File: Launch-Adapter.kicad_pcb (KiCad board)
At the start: 4 copper layers, 81.8 x 144.5 mm, 96 parts, among them J1 ADC1, J2 ADC2, J3 PWM, J4 GPIO, J5 Driver, J6 Measurements, U1 R-785.0-1.0, U2 R-78C3.3-1.0, U3 ISO1050DUB, U4 ADM3490ExR, U5 LMV324

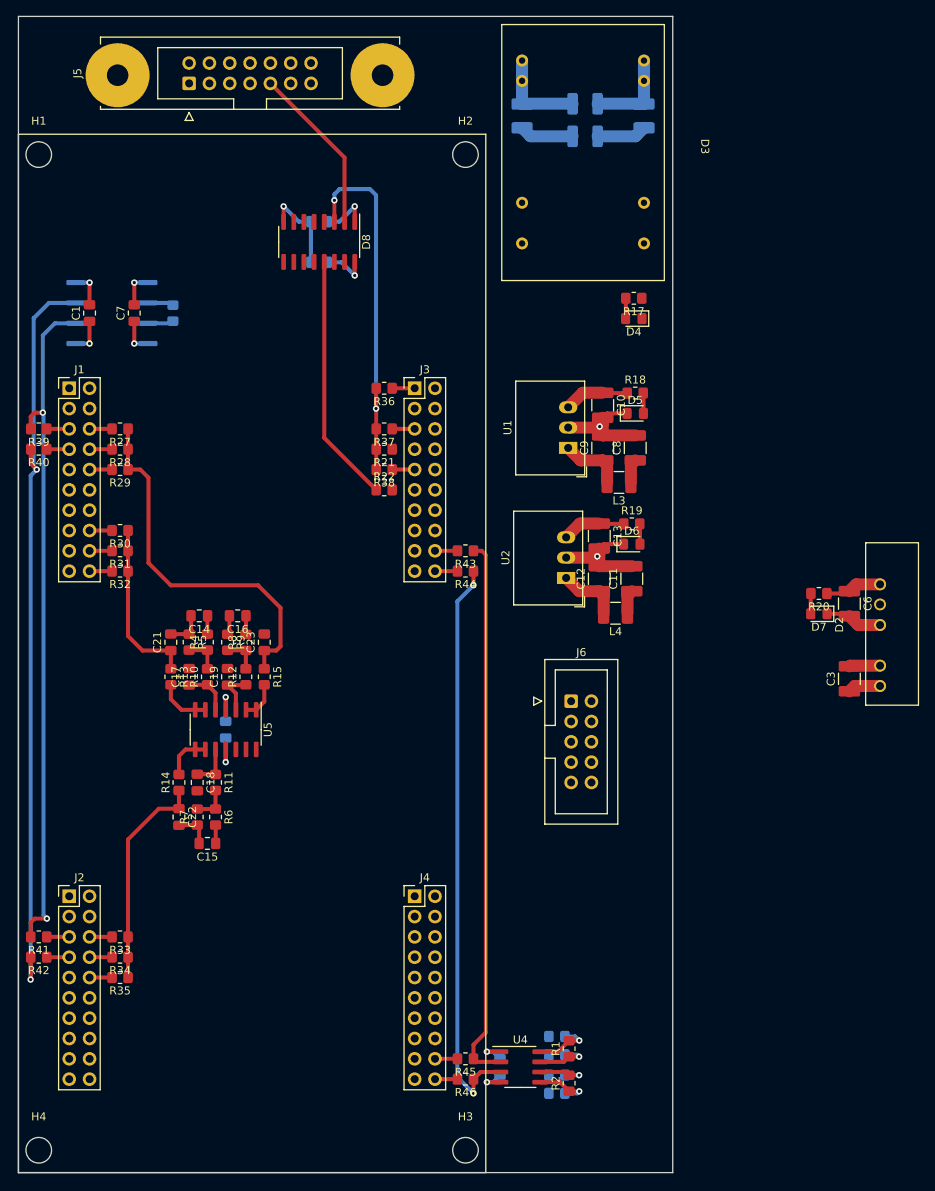
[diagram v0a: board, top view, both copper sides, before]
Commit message: Добавил молексы и убрал питание
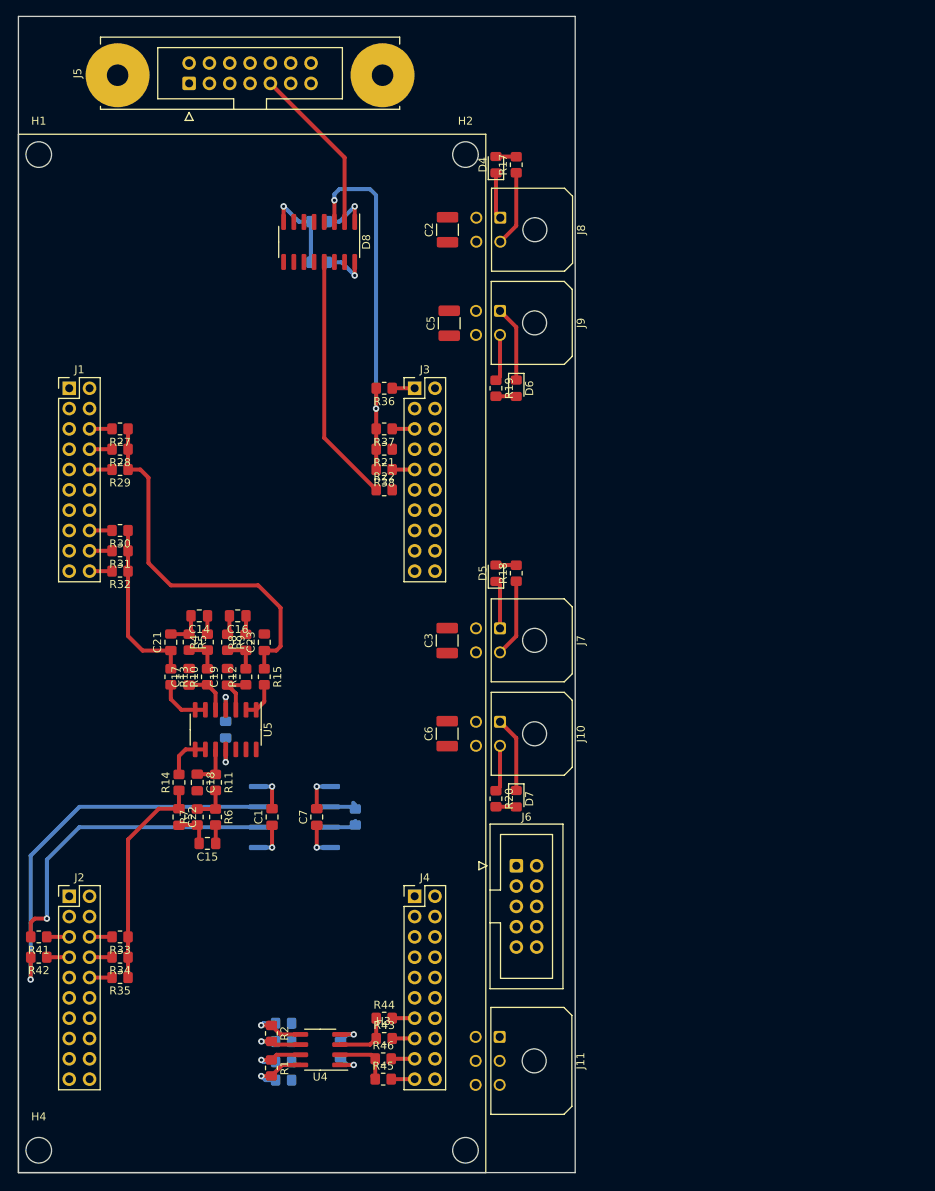
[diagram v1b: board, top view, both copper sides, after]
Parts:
- removed C10, C11, C13, C8: 10u, Capacitor_SMD:C_1210_3225Metric_Pad1.33x2.70mm_HandSolder
- removed C12, C9: 2.2u, Capacitor_SMD:C_1210_3225Metric_Pad1.33x2.70mm_HandSolder
- removed D2: TMA1505S, TRACO_My:TMA1505S
- removed D3: TEN3_2413WI, TRACO_My:TEN3_2413
- removed L1, L2: 150u, Inductor_SMD:L_1210_3225Metric_Pad1.42x2.65mm_HandSolder
- removed L3, L4: 5.6u, Inductor_SMD:L_1210_3225Metric_Pad1.42x2.65mm_HandSolder
- removed R39, R40: 0, Resistor_SMD:R_0805_2012Metric_Pad1.20x1.40mm_HandSolder
- removed U1: R-785.0-1.0, Converter_DCDC:Converter_DCDC_RECOM_R-78E-0.5_THT
- removed U2: R-78C3.3-1.0, Converter_DCDC:Converter_DCDC_RECOM_R-78E-0.5_THT
- added J10: +5V_CAN, Connector_Molex:Molex_Micro-Fit_3.0_43045-0400_2x02_P3.00mm_Horizontal, F.Cu at (116.8, 105.4)
- added J11: Input, Connector_Molex:Molex_Micro-Fit_3.0_43045-0600_2x03_P3.00mm_Horizontal, F.Cu at (116.8, 144.8)
- added J7: +5V, Connector_Molex:Molex_Micro-Fit_3.0_43045-0400_2x02_P3.00mm_Horizontal, F.Cu at (116.8, 93.8)
- added J8: +15V, Connector_Molex:Molex_Micro-Fit_3.0_43045-0400_2x02_P3.00mm_Horizontal, F.Cu at (116.9, 42.4)
- added J9: +3.3V, Connector_Molex:Molex_Micro-Fit_3.0_43045-0400_2x02_P3.00mm_Horizontal, F.Cu at (116.8, 54.1)
- C2, C5: value 4.7u -> 10u; moved to F.Cu
- moved C1 67.0 mm to (88.3, 117.3)
- moved C7 67.0 mm to (93.9, 117.3)
- moved R3 67.0 mm to (98.8, 117.3)
- moved U3 67.0 mm to (91.1, 117.3)
- moved R43 61.8 mm to (102.4, 145.0), turned to 0 degrees
- moved R44 56.8 mm to (102.4, 142.5), turned to 0 degrees
- moved C6 52.8 mm to (110.2, 106.9), turned to 90 degrees
- moved C3 50.5 mm to (110.2, 95.3)
- moved R20 47.8 mm to (116.3, 115.1), turned to -90 degrees
- moved D7 44.3 mm to (118.9, 115.1), turned to -90 degrees
- moved R2 37.7 mm to (88.3, 144.4), turned to -90 degrees
- moved R1 37.3 mm to (88.3, 148.7), turned to -90 degrees
- moved R24 35.3 mm to (89.8, 143.1), turned to 180 degrees
- moved R26 34.6 mm to (89.8, 150.2), turned to 0 degrees
- moved R25 34.4 mm to (89.8, 145.4), turned to 0 degrees
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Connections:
- C2 pad 1: V_IN_SUPPLY -> +15V
- C2 pad 2: GNDD -> GND
- C3 pad 1: +15V -> +5V
- C5 pad 1: Net-(C5-Pad1) -> +3V3
- C5 pad 2: Net-(C5-Pad2) -> GND
- J1 pad 5: Net-(J1-Pad5) -> unconnected-(J1-Pad5)
- J1 pad 7: Net-(J1-Pad7) -> unconnected-(J1-Pad7)
- J3 pad 18: Net-(J3-Pad18) -> unconnected-(J3-Pad18)
- J3 pad 20: Net-(J3-Pad20) -> unconnected-(J3-Pad20)
- J4 pad 13: unconnected-(J4-Pad13) -> Net-(J4-Pad13)
- J4 pad 15: unconnected-(J4-Pad15) -> Net-(J4-Pad15)
- J4 pad 17: unconnected-(J4-Pad17) -> Net-(J4-Pad17)
- J4 pad 18: Net-(J4-Pad18) -> unconnected-(J4-Pad18)
- J4 pad 19: unconnected-(J4-Pad19) -> Net-(J4-Pad19)
- J4 pad 20: Net-(J4-Pad20) -> unconnected-(J4-Pad20)
- R43 pad 1: RO -> DI
- R43 pad 2: Net-(J3-Pad18) -> Net-(J4-Pad15)
- R44 pad 2: Net-(J3-Pad20) -> Net-(J4-Pad13)
- R45 pad 2: Net-(J4-Pad18) -> Net-(J4-Pad19)
- R46 pad 1: DI -> RO
- R46 pad 2: Net-(J4-Pad20) -> Net-(J4-Pad17)
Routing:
- net DI: track 72.5 -> 7.38 mm, vias 2 -> 0
- net RO: track 68.9 -> 7.70 mm
- net RXD: track 85.1 -> 39.5 mm, vias 2 -> 1
- net TXD: track 94.8 -> 49.3 mm, vias 2 -> 1
- net Net-(C5-Pad2): track 11.8 -> 0.00 mm
- net Net-(C5-Pad1): track 11.3 -> 0.00 mm
- net GND: track 67.6 -> 57.3 mm, vias 6 -> 4
- net Net-(C9-Pad1): track 7.95 -> 0.00 mm
- net Net-(C12-Pad1): track 7.81 -> 0.00 mm
- net GNDD: track 6.75 -> 0.00 mm
- net V_IN_SUPPLY: track 6.24 -> 0.00 mm
- net Net-(J4-Pad20): track 2.81 -> 0.00 mm
- net Net-(J4-Pad19): track 0.00 -> 2.81 mm
- net Net-(J4-Pad18): track 2.81 -> 0.00 mm
- net Net-(J4-Pad17): track 0.00 -> 2.81 mm
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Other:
- board size 81.8 x 144.5 mm -> 69.6 x 144.5 mm

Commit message: Первая версия в производство
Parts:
- added D1: PVT412LSPBF, Package_DIP:DIP-6_W8.89mm_SMDSocket_LongPads, F.Cu at (75.4, 45.0)
- added D2: D_Small, Diode_SMD:D_SOD-323F, F.Cu at (79.2, 35.1)
- added J12: Current Measure, Connector_Molex:Molex_Micro-Fit_3.0_43045-0400_2x02_P3.00mm_Horizontal, F.Cu at (126.8, 129.9)
- added J13: Current Measure, Connector_Molex:Molex_Micro-Fit_3.0_43045-0400_2x02_P3.00mm_Horizontal, F.Cu at (126.9, 24.2)
- added Q1: BC817, Package_TO_SOT_SMD:SOT-23, F.Cu at (75.4, 54.6)
- added R16: 4.7k, Resistor_SMD:R_0805_2012Metric_Pad1.20x1.40mm_HandSolder, F.Cu at (74.4, 62.5)
- added R39: 10k, Resistor_SMD:R_0805_2012Metric_Pad1.20x1.40mm_HandSolder, F.Cu at (75.4, 58.7)
- added R40: 220, Resistor_SMD:R_0805_2012Metric_Pad1.20x1.40mm_HandSolder, F.Cu at (71.9, 57.7)
- added R47: 10k, Resistor_SMD:R_0805_2012Metric_Pad1.20x1.40mm_HandSolder, F.Cu at (89.7, 39.4)
- J11: value Input -> Interfaces; footprint Connector_Molex:Molex_Micro-Fit_3.0_43045-0600_2x03_P3.00mm_Horizontal -> Connector_Molex:Molex_Micro-Fit_3.0_43045-0800_2x04_P3.00mm_Horizontal
- J6: value Measurements -> Voltage measure; footprint Connector_IDC:IDC-Header_2x05_P2.54mm_Vertical -> Connector_Molex:Molex_Micro-Fit_3.0_43045-0400_2x02_P3.00mm_Horizontal
- R41: value 0 -> 60
- R42: value 0 -> 10k
- moved R42 102.4 mm to (89.7, 37.1), turned to 0 degrees
- moved R41 90.4 mm to (82.3, 45.0)
- moved R21 38.7 mm to (89.7, 34.8), turned to 0 degrees
- moved D5 21.2 mm to (134.4, 75.7), turned to 0 degrees
- moved R20 19.9 mm to (134.4, 106.7), turned to 0 degrees
- moved D7 19.0 mm to (134.4, 104.1), turned to 0 degrees
- moved D4 18.1 mm to (134.4, 34.0), turned to 0 degrees
- moved R19 18.1 mm to (134.4, 65.3), turned to 0 degrees
- moved R18 17.7 mm to (134.4, 78.2), turned to 0 degrees
- moved R17 15.5 mm to (134.4, 36.6), turned to 0 degrees
- moved D6 15.5 mm to (134.4, 62.7), turned to 0 degrees
- moved C3 14.1 mm to (120.2, 85.3)
- moved C6 14.1 mm to (120.2, 96.9)
- moved J10 14.1 mm to (126.8, 95.4)
- moved J7 14.1 mm to (126.8, 83.8)
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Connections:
- D8 pad 4: unconnected-(D8-Pad4) -> nERR_IN
- D8 pad 5: unconnected-(D8-Pad5) -> nERR_IN_GPIO
- D8 pad 6: unconnected-(D8-Pad6) -> RESET
- D8 pad 7: unconnected-(D8-Pad7) -> RESET_GPIO
- J1 pad 5: unconnected-(J1-Pad5) -> TXD
- J1 pad 7: unconnected-(J1-Pad7) -> RXD
- J11 pad 1: unconnected-(J11-Pad1) -> CANL
- J11 pad 2: unconnected-(J11-Pad2) -> V_IN_PWR
- J11 pad 3: unconnected-(J11-Pad3) -> B
- J11 pad 4: unconnected-(J11-Pad4) -> Y
- J11 pad 5: unconnected-(J11-Pad5) -> CANH
- J11 pad 6: unconnected-(J11-Pad6) -> GNDD
- J2 pad 5: Net-(J2-Pad5) -> unconnected-(J2-Pad5)
- J2 pad 7: Net-(J2-Pad7) -> unconnected-(J2-Pad7)
- J3 pad 13: unconnected-(J3-Pad13) -> RESET_GPIO
- J3 pad 15: unconnected-(J3-Pad15) -> nERR_IN_GPIO
- J3 pad 18: unconnected-(J3-Pad18) -> Relay_Control
- J4 pad 11: unconnected-(J4-Pad11) -> Net-(J4-Pad11)
- J4 pad 17: Net-(J4-Pad17) -> unconnected-(J4-Pad17)
- J4 pad 19: Net-(J4-Pad19) -> unconnected-(J4-Pad19)
- J4 pad 9: unconnected-(J4-Pad9) -> Net-(J4-Pad9)
- J6 pad 1: unconnected-(J6-Pad1) -> GND
- J6 pad 2: unconnected-(J6-Pad2) -> GND
- J6 pad 3: unconnected-(J6-Pad3) -> V_IN
- J6 pad 4: unconnected-(J6-Pad4) -> V_OUT
- R23 pad 1: GND -> GNDD
- R24 pad 1: GND -> GNDD
- R41 pad 1: Net-(J2-Pad5) -> +15V
- R41 pad 2: RXD -> Net-(D1-Pad6)
- R42 pad 1: Net-(J2-Pad7) -> GND
- R42 pad 2: TXD -> nERR_IN_GPIO
- R43 pad 2: Net-(J4-Pad15) -> Net-(J4-Pad11)
- R44 pad 2: Net-(J4-Pad13) -> Net-(J4-Pad9)
- R45 pad 2: Net-(J4-Pad19) -> Net-(J4-Pad15)
- R46 pad 2: Net-(J4-Pad17) -> Net-(J4-Pad13)
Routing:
- net V_IN_PWR: track 0.00 -> 67.9 mm, vias 0 -> 1
- net Relay_Control: track 0.00 -> 65.4 mm
- net nERR_IN_GPIO: track 0.00 -> 63.9 mm, vias 0 -> 1
- net Y: track 7.26 -> 68.7 mm
- net V_OUT: track 2.29 -> 60.7 mm, vias 0 -> 1
- net RESET_GPIO: track 0.00 -> 54.0 mm, vias 0 -> 1
- net Z: track 6.85 -> 60.8 mm
- net I_INDUCT: track 2.31 -> 55.6 mm
- net B: track 7.02 -> 60.0 mm
- net V_IN: track 2.33 -> 54.7 mm, vias 0 -> 1
- net GNDD: track 0.00 -> 49.4 mm, vias 0 -> 1
- net CANL: track 3.21 -> 50.5 mm
- net A: track 7.47 -> 52.5 mm
- net CANH: track 3.21 -> 46.5 mm
- net GND: track 57.3 -> 93.5 mm, vias 4 -> 20
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- added copper zone on F.Cu, net +15V
- added copper zone on F.Cu, net +3V3
- added copper zone on In1.Cu, net +3V3
- added copper zone on F.Cu, net +5V
- added copper zone on In2.Cu, net +5V
- added copper zone on F.Cu, net +5VD
- added copper zone on B.Cu, net GND
- added copper zone on F.Cu, net GND
- added copper zone on F.Cu, net GND2
- added copper zone on In1.Cu, net Net-(D1-Pad4)
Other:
- board size 69.6 x 144.5 mm -> 80.3 x 142.5 mm
- board text added: "+"
- board text added: "+15V"
- board text added: "+3.3V"
- board text added: "+5V"
- board text added: "-"
- board text added: "5V CAN"
- board text added: "Current Measure"
- board text added: "Driver Connector"
- board text added: "RS-485/CAN"
- board text added: "Relay"
- board text added: "Voltage Measure"

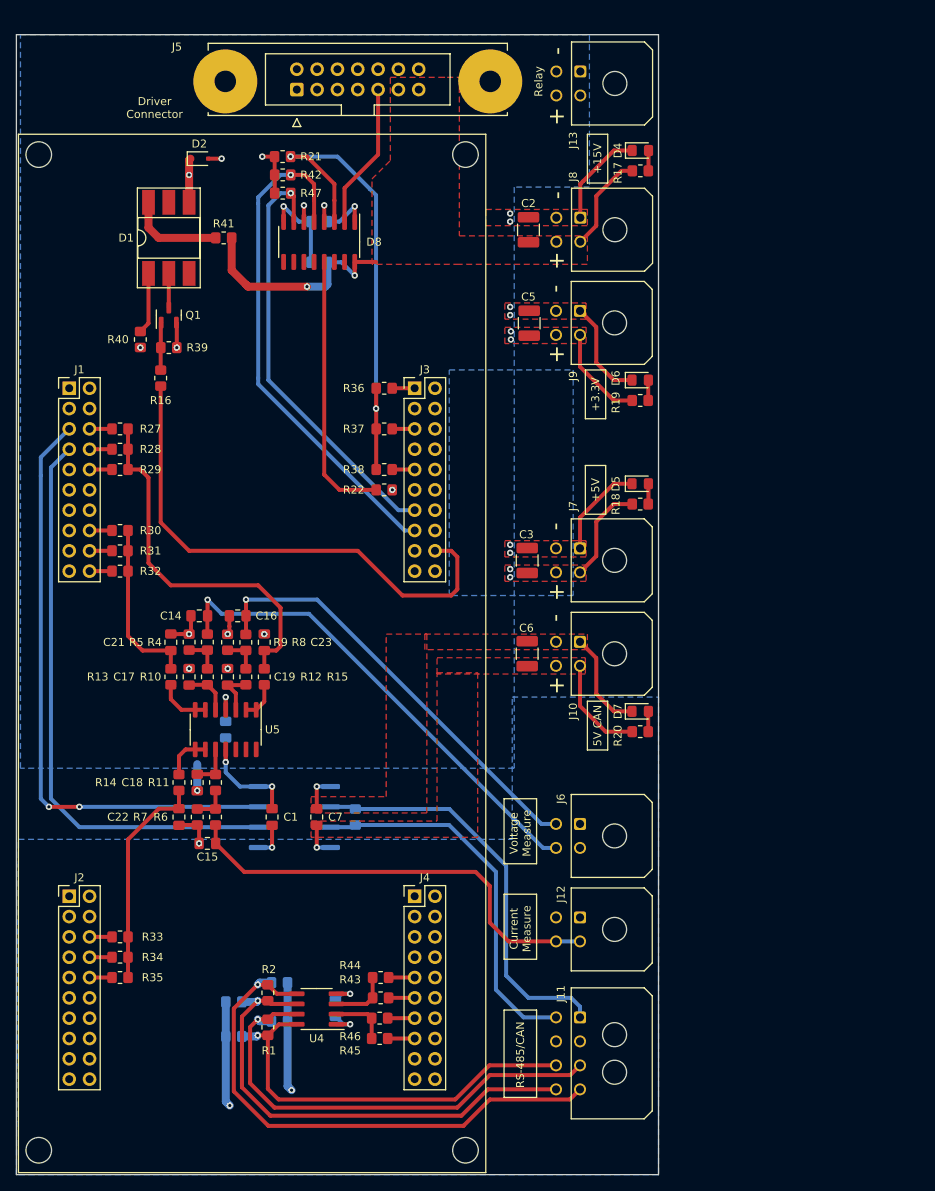
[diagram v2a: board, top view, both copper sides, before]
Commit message: Добавил температуру, убрал подтяжки RS-485, заменил ШИМ на дифференциальный сигнал, добавил земли RS-485
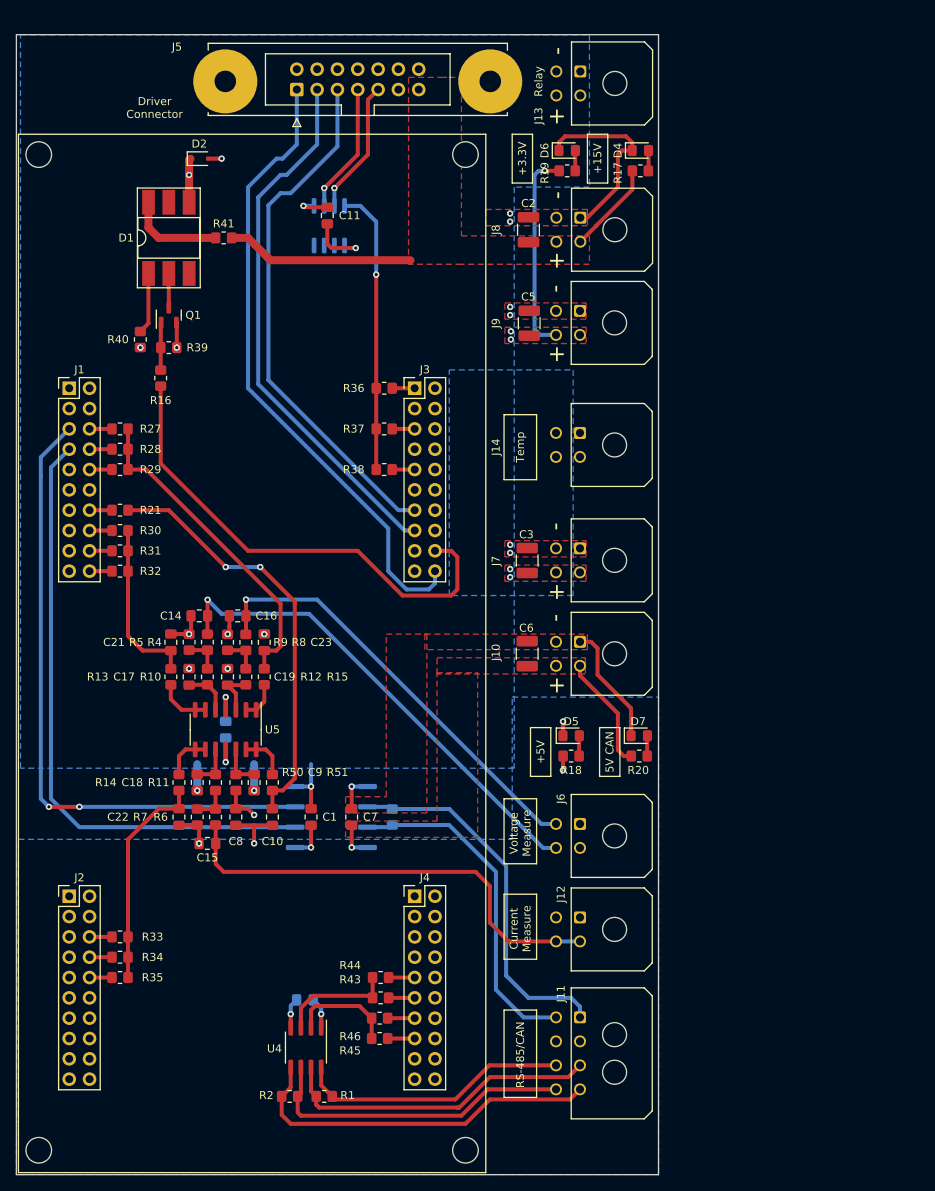
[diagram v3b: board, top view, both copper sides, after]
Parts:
- removed C24, C25: 100n, Capacitor_SMD:C_0805_2012Metric_Pad1.18x1.45mm_HandSolder
- removed D8: CD4504B, Package_SO:SOP-16_3.9x9.9mm_P1.27mm
- removed R22: 1k, Resistor_SMD:R_0805_2012Metric_Pad1.20x1.40mm_HandSolder
- removed R23, R24, R25, R26: 120, Resistor_SMD:R_0805_2012Metric_Pad1.20x1.40mm_HandSolder
- removed R42, R47: 10k, Resistor_SMD:R_0805_2012Metric_Pad1.20x1.40mm_HandSolder
- added C10: 0.27u, Capacitor_SMD:C_0805_2012Metric_Pad1.18x1.45mm_HandSolder, F.Cu at (88.4, 117.3)
- added C11: 100n, Capacitor_SMD:C_0805_2012Metric_Pad1.18x1.45mm_HandSolder, F.Cu at (95.2, 42.2)
- added C8: 1n, Capacitor_SMD:C_0805_2012Metric_Pad1.18x1.45mm_HandSolder, F.Cu at (83.8, 117.3)
- added C9: 10p, Capacitor_SMD:C_0805_2012Metric_Pad1.18x1.45mm_HandSolder, F.Cu at (86.1, 113.0)
- added D3: DS90C401M, Package_SO:SOIC-8_3.9x4.9mm_P1.27mm, B.Cu at (95.5, 43.4)
- added J14: +5V, Connector_Molex:Molex_Micro-Fit_3.0_43045-0400_2x02_P3.00mm_Horizontal, F.Cu at (126.8, 69.3)
- added R50: 100, Resistor_SMD:R_0805_2012Metric_Pad1.20x1.40mm_HandSolder, F.Cu at (83.8, 113.0)
- added R51: 49.9, Resistor_SMD:R_0805_2012Metric_Pad1.20x1.40mm_HandSolder, F.Cu at (88.4, 113.0)
- R21: value 10k -> 0
- moved R21 48.6 mm to (69.3, 79.0), turned to 180 degrees
- moved D5 32.7 mm to (125.7, 107.2)
- moved R18 32.7 mm to (125.7, 109.7)
- moved R19 30.1 mm to (125.2, 36.6)
- moved D6 30.1 mm to (125.2, 34.0)
- moved R2 13.2 mm to (90.6, 152.3), turned to 0 degrees
- moved R1 11.1 mm to (94.9, 152.3), turned to 0 degrees
- moved U4 5.01 mm to (92.6, 146.2), turned to -90 degrees
- moved C1 4.87 mm to (93.2, 117.3)
- moved R3 4.62 mm to (103.4, 117.3)
- moved U3 4.62 mm to (95.8, 117.3)
- moved C7 4.36 mm to (98.3, 117.3)
- moved C4 3.95 mm to (92.5, 140.2), turned to 180 degrees
- moved D7 3.05 mm to (134.2, 107.2)
- moved R20 3.05 mm to (134.2, 109.7)
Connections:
- J1 pad 14: unconnected-(J1-Pad14) -> Net-(J1-Pad14)
- J11 pad 2: V_IN_PWR -> GND
- J11 pad 6: GNDD -> GND
- J3 pad 13: RESET_GPIO -> RST
- J3 pad 15: nERR_IN_GPIO -> FLT
- J3 pad 20: unconnected-(J3-Pad20) -> RDY
- J5 pad 1: RESET -> RDY
- J5 pad 11: +15V -> +5V
- J5 pad 3: nERR_IN -> FLT
- J5 pad 5: nERR_OUT -> RST
- J5 pad 7: unconnected-(J5-Pad7) -> IN-
- J5 pad 9: PWM_OUT -> IN+
- R21 pad 1: GND -> Temp_ADC
- R21 pad 2: PWM_IN -> Net-(J1-Pad14)
- U5 pad 12: unconnected-(U5-Pad12) -> Net-(C9-Pad1)
- U5 pad 13: unconnected-(U5-Pad13) -> Net-(R51-Pad2)
- U5 pad 14: unconnected-(U5-Pad14) -> Net-(R51-Pad2)
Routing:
- net RDY: track 0.00 -> 79.1 mm
- net V_IN_PWR: track 67.9 -> 0.00 mm, vias 1 -> 0
- net FLT: track 0.00 -> 67.5 mm
- net Temp: track 0.00 -> 66.5 mm, vias 0 -> 1
- net RST: track 0.00 -> 65.7 mm
- net nERR_IN_GPIO: track 63.9 -> 0.00 mm, vias 1 -> 0
- net RESET_GPIO: track 54.0 -> 0.00 mm, vias 1 -> 0
- net Temp_ADC: track 0.00 -> 53.4 mm, vias 0 -> 2
- net GNDD: track 49.4 -> 0.00 mm, vias 1 -> 0
- net Net-(D8-Pad13): track 33.9 -> 0.00 mm
- net PWM_IN: track 61.1 -> 35.7 mm, vias 2 -> 1
- net Y: track 68.7 -> 45.9 mm, vias 1 -> 0
- net Z: track 60.8 -> 39.6 mm, vias 1 -> 0
- net B: track 60.0 -> 40.2 mm, vias 1 -> 0
- net A: track 52.5 -> 34.1 mm, vias 1 -> 0
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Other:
- board text added: "Temp"
